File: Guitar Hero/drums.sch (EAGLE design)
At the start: 8 parts

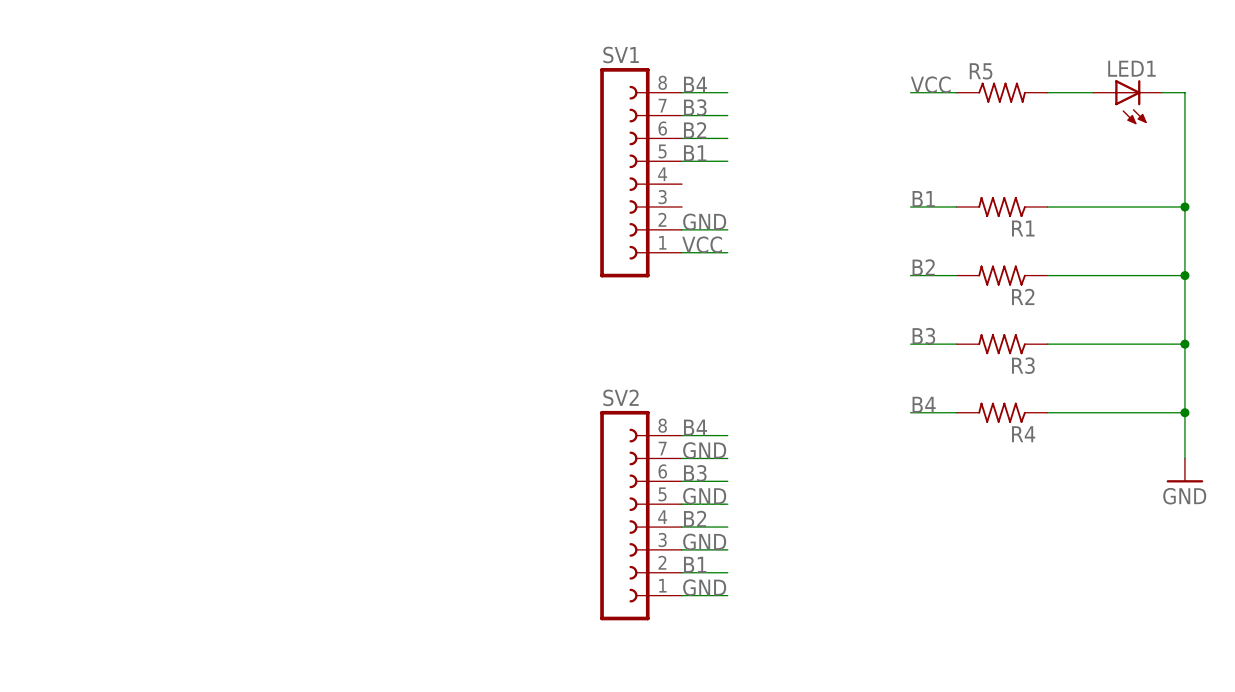
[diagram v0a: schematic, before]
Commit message: Started on base board; made board layout for peripherals
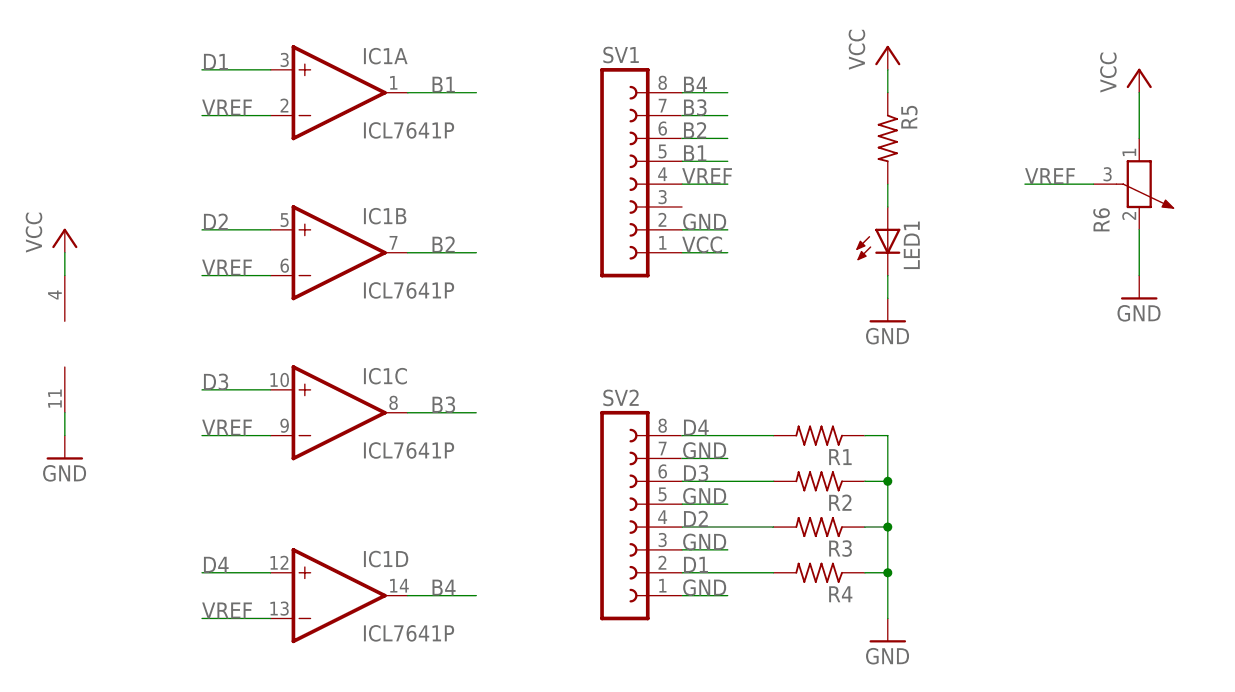
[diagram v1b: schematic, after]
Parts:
- added IC1: ICL7641P, linear:ICL7641P
- added R6: (no value), rcl:POTENTIOMETER_PT_SPIN
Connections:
- new net D1: IC1A.+IN, R4.2, SV2.2
- new net D2: IC1B.+IN, R3.2, SV2.4
- new net D3: IC1C.+IN, R2.2, SV2.6
- new net D4: IC1D.+IN, R1.2, SV2.8
- new net VREF: IC1A.-IN, IC1B.-IN, IC1C.-IN, IC1D.-IN, R6.3, SV1.4
- net B1: now also IC1A.OUT; no longer R1.2, SV2.2
- net B2: now also IC1B.OUT; no longer R2.2, SV2.4
- net B3: now also IC1C.OUT; no longer R3.2, SV2.6
- net B4: now also IC1D.OUT; no longer R4.2, SV2.8
- net GND: now also IC1P.V-, R6.2
- net VCC: now also IC1P.V+, R6.1
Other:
- moved on the sheet: LED1, R1, R2, R3, R4, R5
